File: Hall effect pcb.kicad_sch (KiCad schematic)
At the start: 311 parts, among them J1 USB_C_Receptacle_USB2.0_16P, SW1 SW_SPDT, U1 STM32F411CEU6, U3 AMS1117, U4 USBLC6-2SC6, U5 AMS1117, Y1 16Mhz

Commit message: -Improved analog multiplexer routing
-Connected mux outputs to ADC pins

-Remove 3.3v/3.3va ferrite bead

- Add ferrite bead on LDO inputs for better power filtering
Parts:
- removed C8: 1u, Capacitor_SMD:C_0402_1005Metric, symbol Device:C
- removed H5, H6: MountingHole, MountingHole:MountingHole_3.2mm_M3, symbol Mechanical:MountingHole
- removed SW1: SW_SPDT, Button_Switch_SMD:SW_SPST_B3U-1100P-B, symbol Switch:SW_SPDT
- added D1: RED, LED_SMD:LED_0603_1608Metric, symbol Device:LED
- added R4: 1k5, Resistor_SMD:R_0402_1005Metric, symbol Device:R
- added SW1: SW_Push, Button_Switch_SMD:SW_Tactile_SPST_NO_Straight_CK_PTS636Sx25SMTRLFS, symbol Switch:SW_Push
- AM0:0, AM0:1, AM0:10, AM0:11, AM0:12, AM0:13, AM0:14, AM0:15, AM0:2, AM0:3, AM0:4, AM0:5, AM0:6, AM0:7, AM0:8, AM0:9, AM1:0, AM1:1, AM1:10, AM1:11, AM1:12, AM1:13, AM1:14, AM1:15, AM1:2, AM1:3, AM1:4, AM1:5, AM1:6, AM1:7, AM1:8, AM1:9, AM2:0, AM2:1, AM2:10, AM2:11, AM2:12, AM2:13, AM2:14, AM2:2, AM2:3, AM2:4, AM2:5, AM2:6, AM2:7, AM2:8, AM2:9, AM3:0, AM3:1, AM3:10, AM3:11, AM3:2, AM3:3, AM3:4, AM3:5, AM3:6, AM3:7, AM3:8, AM3:9, AM4:0, AM4:1, AM4:10, AM4:11, AM4:12, AM4:13, AM4:14, AM4:2, AM4:3, AM4:4, AM4:5, AM4:6, AM4:7, AM4:8, AM4:9, AM5:0, AM5:1, AM5:10, AM5:11, AM5:12, AM5:2, AM5:3, AM5:4, AM5:5, AM5:6, AM5:7, AM5:8, AM5:9: footprint Library:gateronkey -> Library:he key
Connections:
- net SW_BOOT0 is gone; now on net GND: R1.1
- net +3.3V: now also D1.2 (A), SW1.1; no longer FB1.2
- net +3.3VA: no longer FB1.1
- net +5V: now also FB1.1; no longer C15.1, U5.3 (VI)
- net AM0: now also U1.16 (PA6); no longer U1.40 (PB4)
- net AM0:0: now also AM0.9 (I0), S21.2 (OUT); no longer AM0.16 (I15), S1.2 (OUT)
- net AM0:1: now also AM0.8 (I1), S22.2 (OUT); no longer AM0.17 (I14), S2.2 (OUT)
- net AM0:10: now also AM0.21 (I10), S2.2 (OUT); no longer AM0.8 (I1), S35.2 (OUT)
- net AM0:11: now also AM0.20 (I11), S1.2 (OUT); no longer AM0.9 (I0), S36.2 (OUT)
- net AM0:12: now also AM0.19 (I12), S17.2 (OUT); no longer AM0.6 (I3), S37.2 (OUT)
- net AM0:13: now also AM0.18 (I13), S18.2 (OUT); no longer AM0.5 (I4), S38.2 (OUT)
- net AM0:14: now also AM0.17 (I14), S19.2 (OUT); no longer AM0.3 (I6), S51.2 (OUT)
- net AM0:15: now also AM0.16 (I15), S20.2 (OUT); no longer AM0.4 (I5), S52.2 (OUT)
- net AM0:2: now also AM0.7 (I2), S23.2 (OUT); no longer AM0.18 (I13), S3.2 (OUT)
- net AM0:3: now also AM0.6 (I3), S24.2 (OUT); no longer AM0.19 (I12), S4.2 (OUT)
- net AM0:4: now also AM0.5 (I4), S25.2 (OUT); no longer AM0.20 (I11), S17.2 (OUT)
- net AM0:5: now also AM0.4 (I5), S7.2 (OUT); no longer AM0.21 (I10), S18.2 (OUT)
- net AM0:6: now also AM0.3 (I6), S6.2 (OUT); no longer AM0.22 (I9), S19.2 (OUT)
- net AM0:7: now also AM0.2 (I7), S5.2 (OUT); no longer AM0.23 (I8), S20.2 (OUT)
- net AM0:8: now also AM0.23 (I8), S4.2 (OUT); no longer AM0.2 (I7), S21.2 (OUT)
- net AM0:9: now also AM0.22 (I9), S3.2 (OUT); no longer AM0.7 (I2), S34.2 (OUT)
- net AM1: now also U1.15 (PA5); no longer U1.41 (PB5)
- net AM1:0: now also AM1.9 (I0), S55.2 (OUT); no longer AM1.19 (I12), S53.2 (OUT)
- net AM1:1: now also AM1.8 (I1), S56.2 (OUT); no longer AM1.20 (I11), S54.2 (OUT)
- net AM1:10: now also AM1.21 (I10), S35.2 (OUT); no longer AM1.2 (I7), S69.2 (OUT)
- net AM1:11: now also AM1.20 (I11), S34.2 (OUT); no longer AM1.3 (I6), S70.2 (OUT)
- net AM1:12: now also AM1.19 (I12), S51.2 (OUT); no longer AM1.9 (I0), S77.2 (OUT)
- net AM1:13: now also AM1.18 (I13), S52.2 (OUT); no longer AM1.8 (I1), S78.2 (OUT)
- net AM1:14: now also AM1.17 (I14), S53.2 (OUT); no longer AM1.7 (I2), S79.2 (OUT)
- net AM1:15: now also AM1.16 (I15), S54.2 (OUT); no longer AM1.5 (I4), S80.2 (OUT)
- net AM1:2: now also AM1.7 (I2), S57.2 (OUT); no longer AM1.21 (I10), S55.2 (OUT)
- net AM1:3: now also AM1.6 (I3), S58.2 (OUT); no longer AM1.22 (I9), S56.2 (OUT)
- net AM1:4: now also AM1.5 (I4), S41.2 (OUT); no longer AM1.23 (I8), S57.2 (OUT)
- net AM1:5: now also AM1.4 (I5), S40.2 (OUT); no longer AM1.18 (I13), S64.2 (OUT)
- net AM1:6: now also AM1.3 (I6), S39.2 (OUT); no longer AM1.17 (I14), S65.2 (OUT)
- net AM1:7: now also AM1.2 (I7), S38.2 (OUT); no longer AM1.16 (I15), S66.2 (OUT)
- net AM1:8: now also AM1.23 (I8), S37.2 (OUT); no longer AM1.6 (I3), S67.2 (OUT)
- net AM1:9: now also AM1.22 (I9), S36.2 (OUT); no longer AM1.4 (I5), S68.2 (OUT)
- net AM2: now also U1.13 (PA3); no longer U1.42 (PB6)
- net AM2:0: now also AM2.9 (I0), S30.2 (OUT); no longer AM2.3 (I6), S5.2 (OUT)
- net AM2:1: now also AM2.8 (I1), S31.2 (OUT); no longer AM2.4 (I5), S6.2 (OUT)
- net AM2:10: now also AM2.21 (I10), S9.2 (OUT); no longer AM2.17 (I14), S39.2 (OUT)
- net AM2:11: now also AM2.20 (I11), S8.2 (OUT); no longer AM2.18 (I13), S40.2 (OUT)
- net AM2:12: now also AM2.19 (I12), S26.2 (OUT); no longer AM2.16 (I15), S41.2 (OUT)
- net AM2:13: now also AM2.18 (I13), S27.2 (OUT); no longer AM2.9 (I0), S42.2 (OUT)
- net AM2:14: now also AM2.17 (I14), S28.2 (OUT); no longer AM2.8 (I1), S43.2 (OUT)
- net AM2:2: now also AM2.7 (I2), S32.2 (OUT); no longer AM2.5 (I4), S7.2 (OUT)
- net AM2:3: now also S16.2 (OUT); no longer S8.2 (OUT)
- net AM2:4: now also AM2.5 (I4), S15.2 (OUT); no longer AM2.7 (I2), S9.2 (OUT)
- net AM2:5: now also AM2.4 (I5), S14.2 (OUT); no longer AM2.19 (I12), S22.2 (OUT)
- net AM2:6: now also AM2.3 (I6), S13.2 (OUT); no longer AM2.20 (I11), S23.2 (OUT)
- net AM2:7: now also AM2.2 (I7), S12.2 (OUT); no longer AM2.21 (I10), S24.2 (OUT)
- net AM2:8: now also S11.2 (OUT); no longer S25.2 (OUT)
- net AM2:9: now also S10.2 (OUT); no longer S26.2 (OUT)
- net AM3: now also U1.12 (PA2); no longer U1.43 (PB7)
- net AM3:1: now also AM3.8 (I1), S63.2 (OUT); no longer AM3.23 (I8), S60.2 (OUT)
- net AM3:10: now also AM3.21 (I10), S43.2 (OUT); no longer AM3.6 (I3), S84.2 (OUT)
- net AM3:11: now also AM3.20 (I11), S42.2 (OUT); no longer AM3.21 (I10), S58.2 (OUT)
- net AM3:2: now also AM3.7 (I2), S50.2 (OUT); no longer AM3.20 (I11), S71.2 (OUT)
- net AM3:3: now also AM3.6 (I3), S33.2 (OUT); no longer AM3.19 (I12), S72.2 (OUT)
- net AM3:4: now also AM3.5 (I4), S49.2 (OUT); no longer AM3.18 (I13), S73.2 (OUT)
- net AM3:5: now also AM3.4 (I5), S48.2 (OUT); no longer AM3.8 (I1), S74.2 (OUT)
- net AM3:6: now also AM3.3 (I6), S47.2 (OUT); no longer AM3.7 (I2), S75.2 (OUT)
- net AM3:7: now also AM3.2 (I7), S46.2 (OUT); no longer AM3.3 (I6), S81.2 (OUT)
- net AM3:8: now also AM3.23 (I8), S45.2 (OUT); no longer AM3.4 (I5), S82.2 (OUT)
- net AM3:9: now also AM3.22 (I9), S44.2 (OUT); no longer AM3.5 (I4), S83.2 (OUT)
- net AM4: now also U1.14 (PA4); no longer U1.45 (PB8)
- net AM4:1: now also AM4.8 (I1), S80.2 (OUT); no longer AM4.19 (I12), S11.2 (OUT)
- net AM4:10: now also AM4.21 (I10), S65.2 (OUT); no longer AM4.7 (I2), S46.2 (OUT)
- net AM4:11: now also AM4.20 (I11), S64.2 (OUT); no longer AM4.6 (I3), S47.2 (OUT)
- net AM4:12: now also AM4.19 (I12), S77.2 (OUT); no longer AM4.3 (I6), S61.2 (OUT)
- net AM4:13: now also AM4.18 (I13), S78.2 (OUT); no longer AM4.4 (I5), S62.2 (OUT)
- net AM4:14: now also AM4.17 (I14), S79.2 (OUT); no longer AM4.5 (I4), S63.2 (OUT)
- net AM4:2: now also AM4.7 (I2), S81.2 (OUT); no longer AM4.20 (I11), S12.2 (OUT)
- net AM4:3: now also AM4.6 (I3), S82.2 (OUT); no longer AM4.21 (I10), S13.2 (OUT)
- net AM4:4: now also AM4.5 (I4), S71.2 (OUT); no longer AM4.17 (I14), S27.2 (OUT)
- net AM4:5: now also AM4.4 (I5), S70.2 (OUT); no longer AM4.22 (I9), S28.2 (OUT)
- net AM4:6: now also AM4.3 (I6), S69.2 (OUT); no longer AM4.23 (I8), S29.2 (OUT)
- net AM4:7: now also S68.2 (OUT); no longer S30.2 (OUT)
- net AM4:8: now also AM4.23 (I8), S67.2 (OUT); no longer AM4.9 (I0), S44.2 (OUT)
- net AM4:9: now also AM4.22 (I9), S66.2 (OUT); no longer AM4.8 (I1), S45.2 (OUT)
- net AM5: now also U1.17 (PA7); no longer U1.46 (PB9)
- net AM5:1: now also AM5.8 (I1), S85.2 (OUT); no longer AM5.21 (I10), S15.2 (OUT)
- net AM5:10: now also AM5.21 (I10), S73.2 (OUT); no longer AM5.6 (I3), S85.2 (OUT)
- net AM5:11: now also AM5.20 (I11), S72.2 (OUT); no longer AM5.7 (I2), S86.2 (OUT)
- net AM5:3: now also AM5.6 (I3), S86.2 (OUT); no longer AM5.17 (I14), S31.2 (OUT)
- net AM5:5: now also S87.2 (OUT); no longer S33.2 (OUT)
- net AM5:7: now also AM5.2 (I7), S76.2 (OUT); no longer AM5.23 (I8), S49.2 (OUT)
- net AM5:8: now also AM5.23 (I8), S75.2 (OUT); no longer AM5.3 (I6), S50.2 (OUT)
- net AM5:9: now also AM5.22 (I9), S74.2 (OUT); no longer AM5.9 (I0), S76.2 (OUT)
- net GND: now also AM4.9 (I0), AM5.17 (I14), AM5.3 (I6), AM5.5 (I4), AM5.7 (I2), AM5.9 (I0), R4.2; no longer AM2.2 (I7), AM3.16 (I15), AM3.17 (I14), AM3.2 (I7), AM5.2 (I7), AM5.20 (I11)
- net SELECT0: now also U1.40 (PB4); no longer U1.25 (PB12)
- net SELECT1: now also U1.39 (PB3); no longer U1.26 (PB13)
- net SELECT2: now also U1.42 (PB6); no longer U1.27 (PB14)
- net SELECT3: now also U1.41 (PB5); no longer U1.28 (PB15)
- net AM3:0 renamed AM3:12
- net AM3:12: now also AM3.19 (I12); no longer AM3.22 (I9)
- removed net AM4:0: AM4.18 (I13), S10.2 (OUT)
- net AM5:0 renamed AM5:15
- net AM5:15: now also S84.2 (OUT); no longer S14.2 (OUT)
- removed net AM5:12: AM5.8 (I1), S87.2 (OUT)
- removed net AM5:2: AM5.5 (I4), S16.2 (OUT)
- removed net AM5:4: AM5.22 (I9), S32.2 (OUT)
- net AM5:6 renamed AM5:13
- net AM5:13: now also S83.2 (OUT); no longer S48.2 (OUT)
- net BOOT0: no longer names the net of R1.2, U1.44 (BOOT0)
- net BOOT0: now also SW1.2
- new net +5VA: C15.1, FB1.2, U5.3 (VI)
- new net AM2:15: AM2.16 (I15), S29.2 (OUT)
- new net AM3:13: AM3.18 (I13), S60.2 (OUT)
- new net AM3:14: AM3.17 (I14), S61.2 (OUT)
- new net AM3:15: AM3.16 (I15), S62.2 (OUT)
- new net PWR_LED_K: D1.1 (K), R4.1
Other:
- moved on the sheet: R1

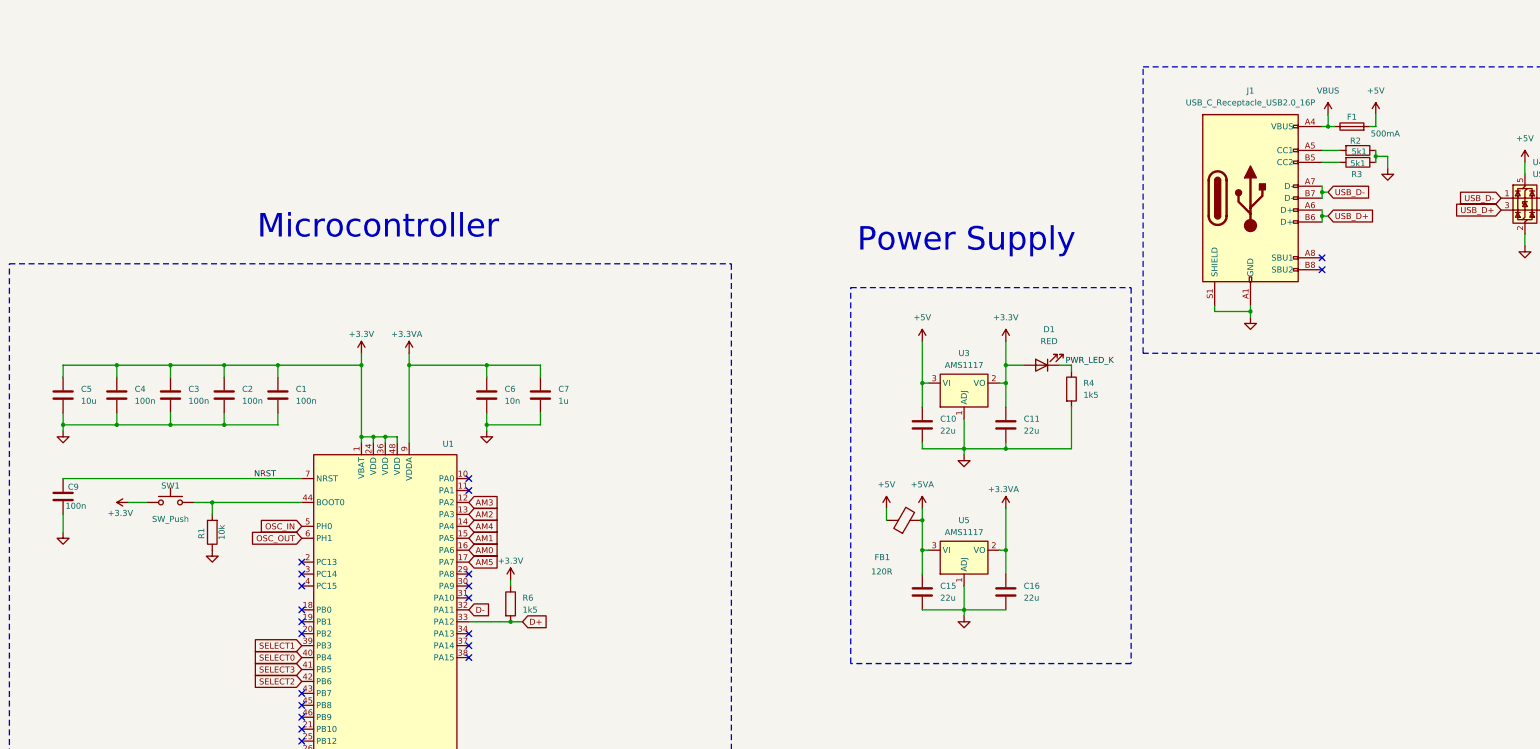
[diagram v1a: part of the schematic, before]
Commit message: added NRST pin
changed boot0 and nrst to SW_SPST

set board to 4 layers and impedance controlled usb data lines for 90 ohm

slight changes to select line routing
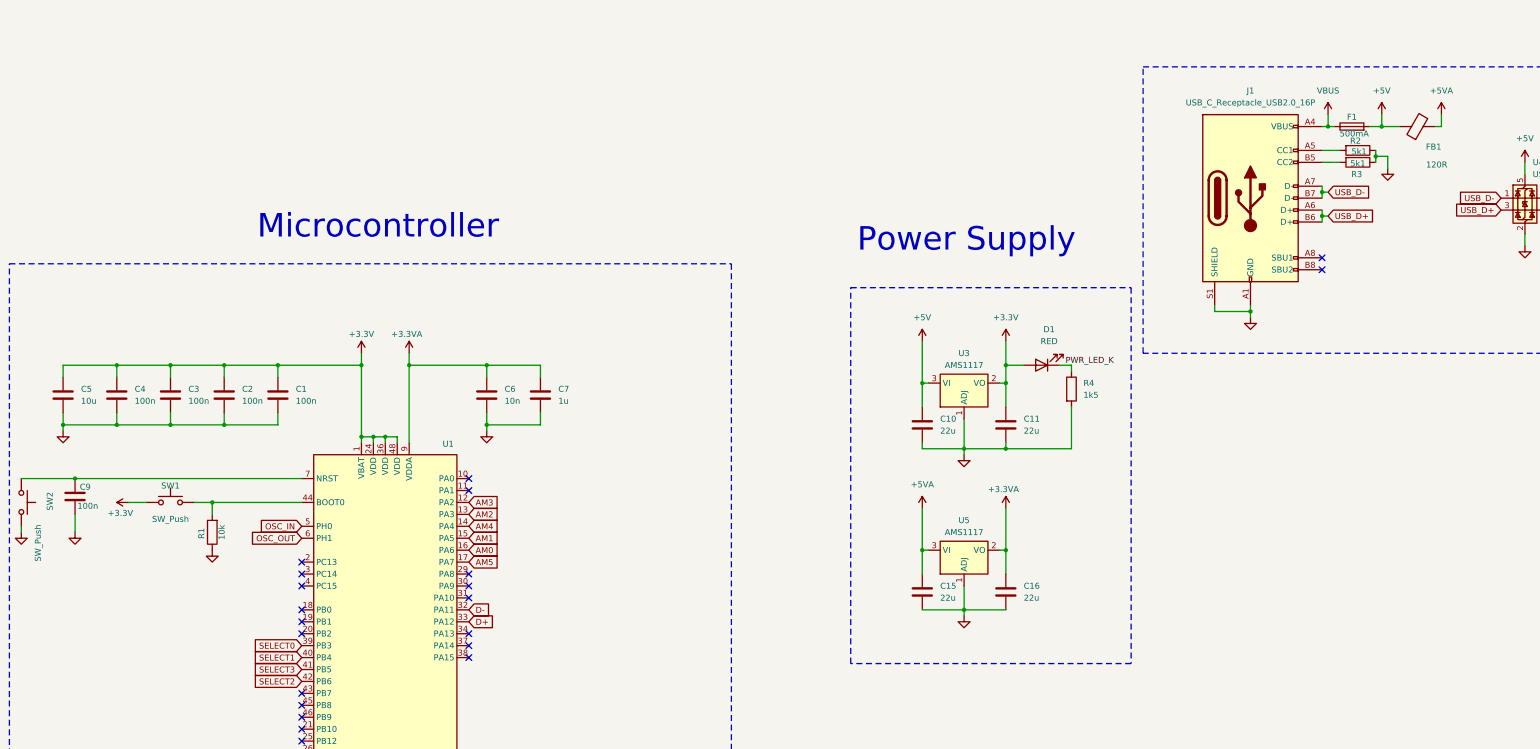
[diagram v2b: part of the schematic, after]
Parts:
- removed R6: 1k5, Resistor_SMD:R_0402_1005Metric, symbol Device:R
- added SW2: SW_Push, Button_Switch_SMD:SW_SPST_CK_RS282G05A3, symbol Switch:SW_Push
- SW1: footprint Button_Switch_SMD:SW_Tactile_SPST_NO_Straight_CK_PTS636Sx25SMTRLFS -> Button_Switch_SMD:SW_SPST_CK_RS282G05A3
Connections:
- net GND: now also SW2.2
- net SELECT0: now also U1.39 (PB3); no longer U1.40 (PB4)
- net SELECT1: now also U1.40 (PB4); no longer U1.39 (PB3)
- net NRST: no longer names the net of C9.1, U1.7 (NRST)
- net NRST: now also SW2.1
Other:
- moved on the sheet: C9, FB1

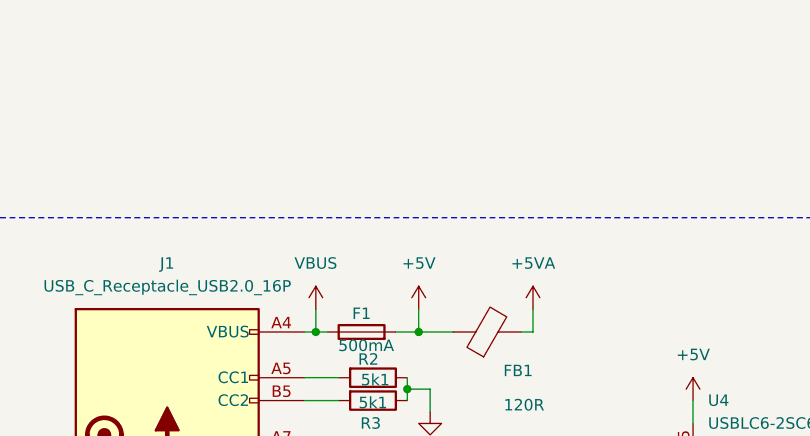
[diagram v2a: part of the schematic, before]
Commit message: removed unused capacitor
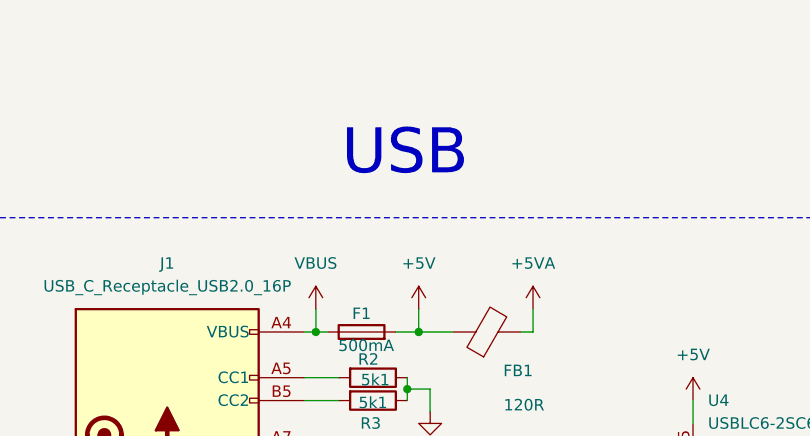
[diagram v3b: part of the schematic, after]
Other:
- note added: "USB"
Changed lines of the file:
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@@
+		)
+	)
+	(text "USB"
+		(exclude_from_sim no)
+		(at 328.676 30.988 0)
+		(effects
+			(font
+				(size 5 5)
+			)
 		)
 	)
